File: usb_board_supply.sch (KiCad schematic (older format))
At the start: 8 parts, among them J1 USB_B_Micro, J2 Conn_01x02, J3 Conn_01x02, SW1 SW_DPST

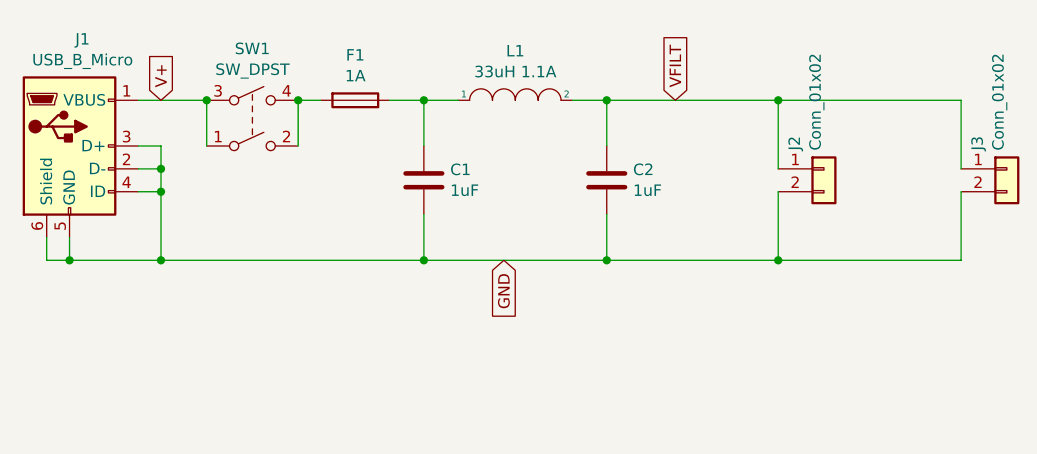
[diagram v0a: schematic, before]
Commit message: Update to use mosfet instead of switch
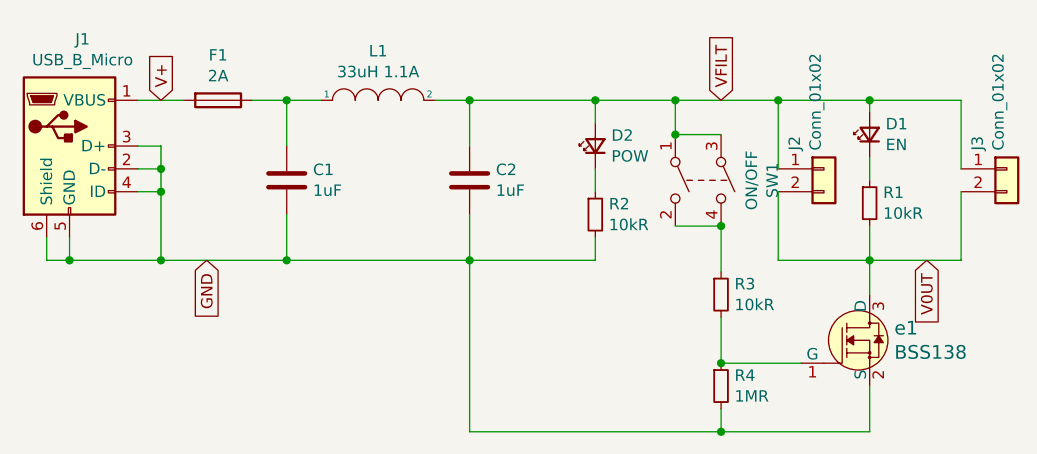
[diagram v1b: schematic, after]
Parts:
- added D1: EN, LED_SMD:LED_0603_1608Metric, symbol Device:LED_Small
- added D2: POW, LED_SMD:LED_0603_1608Metric, symbol Device:LED_Small
- added R1, R2, R3: 10kR, Resistor_SMD:R_0805_2012Metric, symbol Device:R_Small
- added R4: 1MR, Resistor_SMD:R_0805_2012Metric, symbol Device:R_Small
- added e1: BSS138, digikey-footprints:SOT-23-3, symbol dk_Transistors-FETs-MOSFETs-Single:BSS138
- F1: value 1A -> 2A; footprint Fuse:Fuse_0805_2012Metric -> Fuse:Fuse_0603_1608Metric
- SW1: value SW_DPST -> ON/OFF
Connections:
- net GND: now also R2.2, R4.2, e1.2 (S); no longer J2.2 (Pin_2), J3.2 (Pin_2)
- net V+: now also F1.2; no longer SW1.1, SW1.3
- net VFILT: now also SW1.1, SW1.3, D1.2 (A), D2.2 (A)
- net at SW1.2, SW1.4: now also R3.1; no longer F1.2
- new net: D2.1 (K), R2.1
- new net: D1.1 (K), R1.1
- new net: R3.2, R4.1, e1.1 (G)
- new net V0UT: J2.2 (Pin_2), J3.2 (Pin_2), R1.2, e1.3 (D)
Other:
- moved on the sheet: C1, C2, F1, L1, SW1
